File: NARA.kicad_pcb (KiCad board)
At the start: 4 copper layers, 93.9 x 42.4 mm, 144 parts, among them K1 BATT, K10 TOF_LD, K11 TOF_LS, K12 TOF_RF, K13 TOF_RD, K14 TOF_RS, K2 K_FPC_52435-2471, K3 PROG, K5 K_PicoSPOX-3, K6 K_0002, K7 K_PicoSPOX-3, K8 K_0002, K9 TOF_LF, Q1 Q_0004, Q2 Q_0007, Q3 Q_0007, Q4 Q_0007, Q5 Q_0007, Q6 Q_0007, Q7 Q_0007, Q8 Q_0004, Q9 Q_0004, SW1 SW_SKQG, SW2 SW_SKQG, U1 U_LT8610ABIMSE-3.3, U10 QRE1113GR, U11 QRE1113GR, U12 QRE1113GR, U2 U_AP2204K-5.0TRG1, U3 LTC2944, U4 L6234, U5 L6234, U6 LTC2955TS8-1, U7 STM32H743VITx, U8 ICM-20689, U9 QRE1113GR

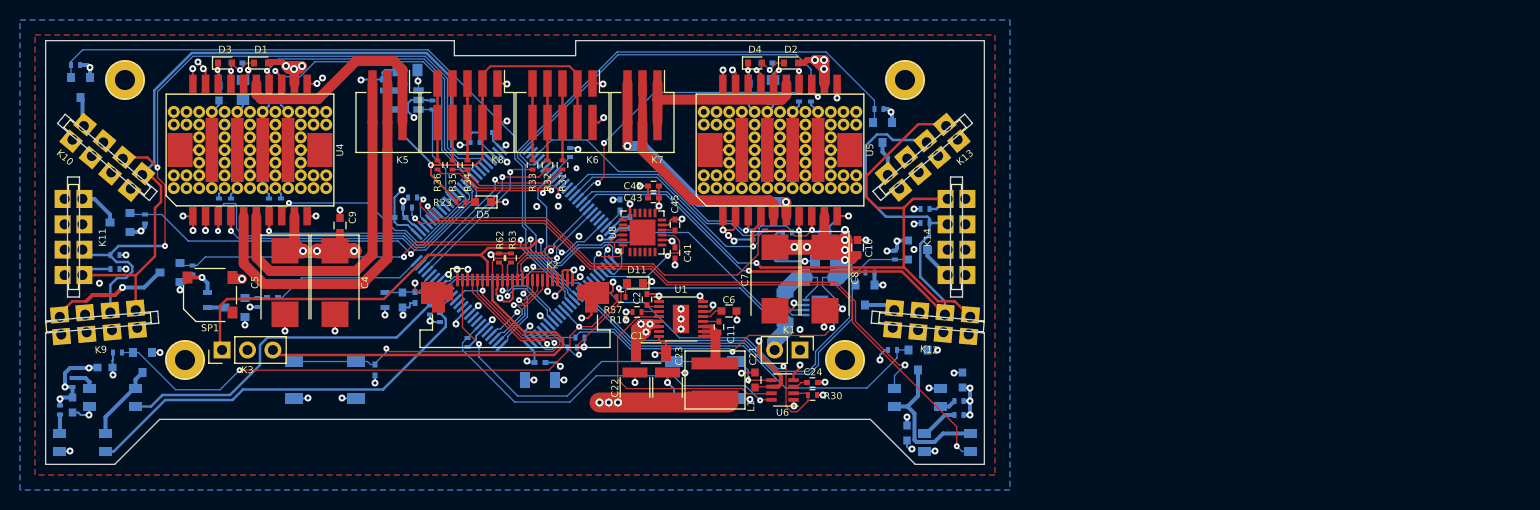
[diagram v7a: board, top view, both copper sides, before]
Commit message: New v1.1.0, add jtag Connector and main led
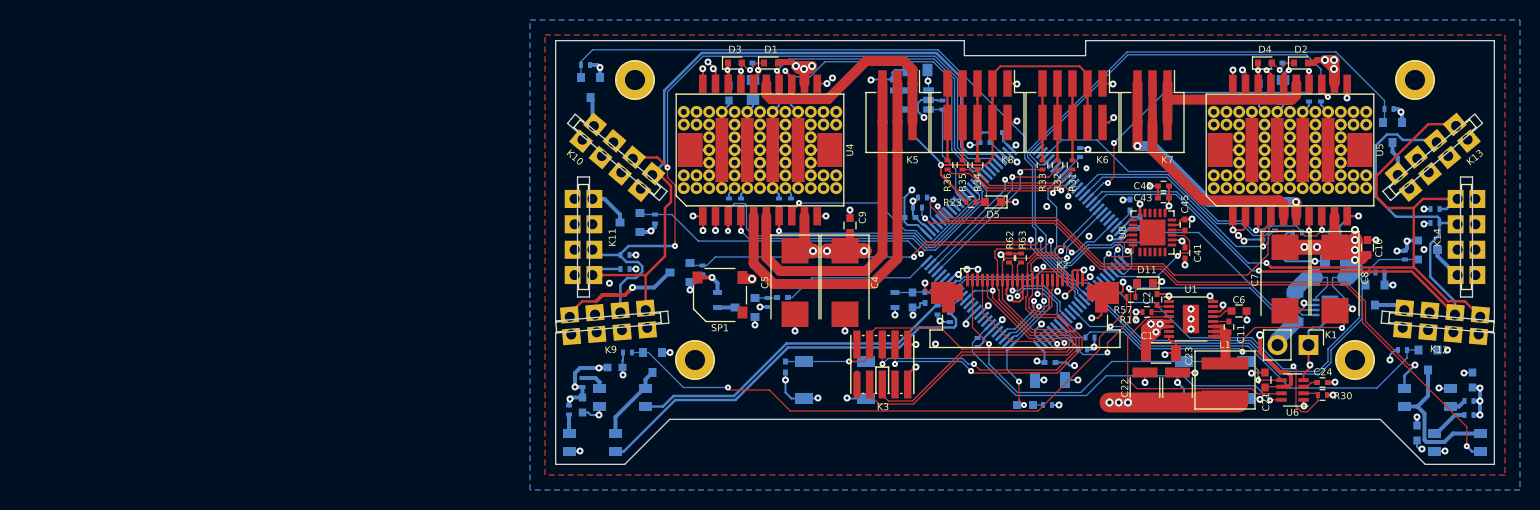
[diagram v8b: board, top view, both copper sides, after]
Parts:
- added D6: D_0001, DVB_LED:LED_0603-red, B.Cu at (149.0, 108.5)
- added G***: LOGO, NARA_Lib:Logo_Pacabot, F.Cu at (124.8, 102.9)
- added G***: LOGO, NARA_Lib:Logo_Nara, F.Cu at (144.3, 107.3)
- added G***: LOGO, NARA_Lib:Logo_Pacabot, B.Cu at (140.3, 107.3)
- added G***: LOGO, NARA_Lib:Logo_Nara, B.Cu at (130.7, 98.9)
- added R19: R_0104, DVB_Resistors:R_0402, B.Cu at (151.2, 108.5)
- K1: footprint DVB_Connectors:Pin_Header_Straight_1x02_Pitch2.54mm -> NARA_Lib:Pin_Header_Straight_1x02_Pitch3mm
- K10: value TOF_LD -> TOF_RD
- K11: value TOF_LS -> TOF_RS
- K12: value TOF_RF -> TOF_LF
- K13: value TOF_RD -> TOF_LD
- K14: value TOF_RS -> TOF_LS
- K3: value PROG -> DVB_JTAG-10; footprint DVB_Connectors:Pin_Header_Straight_1x03_Pitch2.54mm -> NARA_Lib:FTSH-105-XX-X-DV
- K9: value TOF_LF -> TOF_RF
- moved K3 66.0 mm to (134.7, 104.5), turned to 180 degrees
- moved R7 51.0 mm to (154.8, 103.0)
- moved C16 51.0 mm to (174.8, 77.0)
- moved D5 51.0 mm to (145.8, 88.2)
- moved K10 51.0 mm to (108.2, 83.7)
- moved C1 51.0 mm to (162.6, 103.3)
- moved C10 51.0 mm to (183.2, 92.8)
- moved C11 51.0 mm to (169.4, 100.7)
- moved C12 51.0 mm to (121.2, 74.3)
- moved C14 51.0 mm to (135.8, 76.5)
- moved C15 51.0 mm to (121.8, 77.0)
- moved C17 51.0 mm to (180.0, 94.1)
- moved C18 51.0 mm to (119.4, 77.3)
- moved C19 51.0 mm to (172.4, 77.1)
- moved C21 51.0 mm to (173.0, 106.0)
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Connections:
- K10 pad 1: /TOF_L_SDA -> /TOF_R_SDA
- K10 pad 2: /TOF_L_SCL -> /TOF_R_SCL
- K11 pad 1: /TOF_L_SDA -> /TOF_R_SDA
- K11 pad 2: /TOF_L_SCL -> /TOF_R_SCL
- K12 pad 1: /TOF_R_SDA -> /TOF_L_SDA
- K12 pad 2: /TOF_R_SCL -> /TOF_L_SCL
- K13 pad 1: /TOF_R_SDA -> /TOF_L_SDA
- K13 pad 2: /TOF_R_SCL -> /TOF_L_SCL
- K14 pad 1: /TOF_R_SDA -> /TOF_L_SDA
- K14 pad 2: /TOF_R_SCL -> /TOF_L_SCL
- K3 pad 1: /SWCLK -> GND
- K5 pad 1: /MOT_L_PHASE_C_YEL -> /MOT_R_PHASE_C_YEL
- K5 pad 2: /MOT_L_PHASE_B_ORA -> /MOT_R_PHASE_B_ORA
- K5 pad 3: /MOT_L_PHASE_A_BRO -> /MOT_R_PHASE_A_BRO
- K7 pad 1: /MOT_R_PHASE_C_YEL -> /MOT_L_PHASE_C_YEL
- K7 pad 2: /MOT_R_PHASE_B_ORA -> /MOT_L_PHASE_B_ORA
- K7 pad 3: /MOT_R_PHASE_A_BRO -> /MOT_L_PHASE_A_BRO
- K9 pad 1: /TOF_L_SDA -> /TOF_R_SDA
- K9 pad 2: /TOF_L_SCL -> /TOF_R_SCL
- Q2 pad 1: /TOF_EN_LF -> /TOF_EN_RF
- Q3 pad 1: /TOF_EN_LD -> /TOF_EN_RD
- Q4 pad 1: /TOF_EN_LS -> /TOF_EN_RS
- Q5 pad 1: /TOF_EN_RF -> /TOF_EN_LF
- Q6 pad 1: /TOF_EN_RD -> /TOF_EN_LD
- Q7 pad 1: /TOF_EN_RS -> /TOF_EN_LS
- R1 pad 2: /MOT_L_IN1 -> /MOT_R_IN1
- R10 pad 2: /MOT_R_EN1 -> /MOT_L_EN1
- R12 pad 2: /MOT_L_EN2 -> /MOT_R_EN2
- R13 pad 2: /MOT_R_EN2 -> /MOT_L_EN2
- R15 pad 2: /MOT_L_EN3 -> /MOT_R_EN3
- R16 pad 2: /MOT_R_EN3 -> /MOT_L_EN3
- R2 pad 2: /MOT_R_IN1 -> /MOT_L_IN1
- R3 pad 2: /MOT_L_IN2 -> /MOT_R_IN2
- R31 pad 2: /MOT_L_HALL3 -> /MOT_R_HALL3
- R32 pad 2: /MOT_L_HALL2 -> /MOT_R_HALL2
- R33 pad 2: /MOT_L_HALL1 -> /MOT_R_HALL1
- R34 pad 2: /MOT_R_HALL3 -> /MOT_L_HALL3
- R35 pad 2: /MOT_R_HALL2 -> /MOT_L_HALL2
- R36 pad 2: /MOT_R_HALL1 -> /MOT_L_HALL1
- R39 pad 2: /TOF_EN_LF -> /TOF_EN_RF
- R4 pad 2: /MOT_R_IN2 -> /MOT_L_IN2
- R40 pad 2: /TOF_EN_LD -> /TOF_EN_RD
- R41 pad 2: /TOF_EN_LS -> /TOF_EN_RS
- R42 pad 2: /TOF_EN_RF -> /TOF_EN_LF
- R43 pad 2: /TOF_EN_RD -> /TOF_EN_LD
- R44 pad 2: /TOF_EN_RS -> /TOF_EN_LS
- R5 pad 2: /MOT_L_IN3 -> /MOT_R_IN3
- R53 pad 2: /LINE_ADC_L1 -> /LINE_ADC_R1
- R54 pad 2: /LINE_ADC_L2 -> /LINE_ADC_R2
- R55 pad 2: /LINE_ADC_R1 -> /LINE_ADC_L1
- R56 pad 2: /LINE_ADC_R2 -> /LINE_ADC_L2
- R6 pad 2: /MOT_R_IN3 -> /MOT_L_IN3
- R64 pad 1: /TOF_L_SDA -> /TOF_R_SDA
- R65 pad 2: /TOF_L_SCL -> /TOF_R_SCL
- R66 pad 1: /TOF_R_SDA -> /TOF_L_SDA
- R67 pad 2: /TOF_R_SCL -> /TOF_L_SCL
- R9 pad 2: /MOT_L_EN1 -> /MOT_R_EN1
- U10 pad 3: /LINE_ADC_L2 -> /LINE_ADC_R2
- U11 pad 3: /LINE_ADC_R1 -> /LINE_ADC_L1
- U12 pad 3: /LINE_ADC_R2 -> /LINE_ADC_L2
- U4 pad 13: /MOT_L_EN3 -> /MOT_R_EN3
- U4 pad 14: /MOT_L_IN3 -> /MOT_R_IN3
- U4 pad 15: /MOT_L_PHASE_C_YEL -> /MOT_R_PHASE_C_YEL
- U4 pad 3: /MOT_L_EN2 -> /MOT_R_EN2
- U4 pad 4: /MOT_L_IN2 -> /MOT_R_IN2
- U4 pad 5: /MOT_L_PHASE_B_ORA -> /MOT_R_PHASE_B_ORA
- U4 pad 6: /MOT_L_PHASE_A_BRO -> /MOT_R_PHASE_A_BRO
- U4 pad 7: /MOT_L_IN1 -> /MOT_R_IN1
- U4 pad 8: /MOT_L_EN1 -> /MOT_R_EN1
- U5 pad 13: /MOT_R_EN3 -> /MOT_L_EN3
- U5 pad 14: /MOT_R_IN3 -> /MOT_L_IN3
- U5 pad 15: /MOT_R_PHASE_C_YEL -> /MOT_L_PHASE_C_YEL
- U5 pad 3: /MOT_R_EN2 -> /MOT_L_EN2
- U5 pad 4: /MOT_R_IN2 -> /MOT_L_IN2
- U5 pad 5: /MOT_R_PHASE_B_ORA -> /MOT_L_PHASE_B_ORA
- U5 pad 6: /MOT_R_PHASE_A_BRO -> /MOT_L_PHASE_A_BRO
- U5 pad 7: /MOT_R_IN1 -> /MOT_L_IN1
- U5 pad 8: /MOT_R_EN1 -> /MOT_L_EN1
- U7 pad 15: /LINE_ADC_L1 -> /LINE_ADC_R1
- U7 pad 16: /LINE_ADC_L2 -> /LINE_ADC_R2
- U7 pad 22: /MOT_L_HALL1 -> /MOT_R_HALL1
- U7 pad 23: /MOT_L_HALL2 -> /MOT_R_HALL2
- U7 pad 24: /MOT_L_HALL3 -> /MOT_R_HALL3
- U7 pad 28: /LINE_ADC_R1 -> /LINE_ADC_L1
- U7 pad 29: /LINE_ADC_R2 -> /LINE_ADC_L2
- U7 pad 31: /MOT_R_EN1 -> /MOT_L_EN1
- U7 pad 38: /MOT_L_EN1 -> /MOT_R_EN1
- U7 pad 39: /MOT_L_IN1 -> /MOT_R_IN1
- U7 pad 40: /MOT_L_EN2 -> /MOT_R_EN2
- U7 pad 41: /MOT_L_IN2 -> /MOT_R_IN2
- U7 pad 42: /MOT_L_EN3 -> /MOT_R_EN3
- U7 pad 43: /MOT_L_IN3 -> /MOT_R_IN3
- U7 pad 46: /TOF_L_SCL -> /TOF_R_SCL
- U7 pad 47: /TOF_L_SDA -> /TOF_R_SDA
- U7 pad 53: /MOT_R_EN2 -> /MOT_L_EN2
- U7 pad 54: /MOT_R_EN3 -> /MOT_L_EN3
- U7 pad 59: /MOT_R_HALL1 -> /MOT_L_HALL1
- U7 pad 60: /MOT_R_HALL2 -> /MOT_L_HALL2
- U7 pad 61: /MOT_R_HALL3 -> /MOT_L_HALL3
- U7 pad 63: /MOT_R_IN1 -> /MOT_L_IN1
- U7 pad 64: /MOT_R_IN2 -> /MOT_L_IN2
- U7 pad 65: /MOT_R_IN3 -> /MOT_L_IN3
- U7 pad 66: /TOF_R_SDA -> /TOF_L_SDA
- U7 pad 67: /TOF_R_SCL -> /TOF_L_SCL
- U7 pad 83: /TOF_EN_RS -> /TOF_EN_LS
- U7 pad 84: /TOF_EN_RD -> /TOF_EN_LD
- U7 pad 85: /TOF_EN_RF -> /TOF_EN_LF
- U7 pad 86: /TOF_EN_LS -> /TOF_EN_RS
- U7 pad 87: /TOF_EN_LD -> /TOF_EN_RD
- U7 pad 88: /TOF_EN_LF -> /TOF_EN_RF
- U9 pad 3: /LINE_ADC_L1 -> /LINE_ADC_R1
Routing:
- net /BLUETOOTH_TX: track 12.0 -> 45.6 mm, vias 1 -> 3
- net /BLUETOOTH_RX: track 11.5 -> 44.3 mm, vias 1 -> 3
- net /LINE_ADC_R2: track 63.3 -> 36.0 mm, vias 2 -> 0
- net /LINE_ADC_R1: track 70.0 -> 42.9 mm, vias 2 -> 0
- net /LINE_ADC_L1: track 43.0 -> 70.0 mm, vias 0 -> 2
- net /LINE_ADC_L2: track 37.2 -> 63.3 mm, vias 0 -> 2
- net /MOT_R_EN1: track 48.4 -> 24.7 mm, vias 2 -> 1
- net /MOT_L_EN1: track 24.7 -> 48.4 mm, vias 1 -> 2
- net /MOT_R_PHASE_B_ORA: track 23.2 -> 38.5 mm
- net /MOT_L_PHASE_B_ORA: track 38.5 -> 23.2 mm
- net GND: track 834.0 -> 847.2 mm, vias 93 -> 92
- net +3.3V: track 350.0 -> 361.3 mm, vias 41 -> 44
- net /MOT_R_EN2: track 27.7 -> 36.4 mm
- net /MOT_L_EN2: track 36.4 -> 27.7 mm
- net /MOT_R_EN3: track 41.3 -> 32.7 mm
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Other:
- board text added: "+"
- board text added: "HM v1.1.0"
- board text added: "I/O"
- board text added: "PLF 2018"
- board text added: "RST"
